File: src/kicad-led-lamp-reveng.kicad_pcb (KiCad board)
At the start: 2 copper layers, 18 parts, among them J1 AC2, J2 AC1, J3 L+, J4 L-, SW1 SW_Push_SPDT

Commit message: Finished pcb layout
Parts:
- removed the R1 at (84.7, 77.9)
- added R3: 390k, Resistor_THT:R_Axial_DIN0207_L6.3mm_D2.5mm_P7.62mm_Horizontal, F.Cu at (128.3, 85.7)
- D1, D3, D4, D5, D6: footprint Resistor_THT:R_Axial_DIN0207_L6.3mm_D2.5mm_P7.62mm_Horizontal -> igorkelvin:DIODE_Axial_DIN0207_L6.3mm_D2.5mm_P7.62mm_Horizontal
- moved C1 117.6 mm to (178.4, 74.9), turned to 270 degrees
- moved R1 109.5 mm to (183.5, 74.9), turned to 270 degrees
- moved C2 108.4 mm to (168.3, 92.7), turned to 180 degrees
- moved R2 106.4 mm to (167.0, 77.5), turned to 270 degrees
- moved D1 101.2 mm to (172.1, 77.5), turned to 270 degrees
- moved D4 81.0 mm to (142.2, 95.2), turned to 90 degrees
- moved D5 79.3 mm to (139.1, 77.5), turned to 270 degrees
- moved SW1 75.7 mm to (149.2, 85.1)
- moved D6 67.4 mm to (139.1, 95.2), turned to 90 degrees
- moved D2 64.3 mm to (159.4, 71.1), turned to 180 degrees
- moved J2 62.0 mm to (145.4, 88.9)
- moved J1 61.4 mm to (147.3, 75.6)
- moved R4 60.8 mm to (145.4, 77.5), turned to 270 degrees
- moved D3 48.1 mm to (142.2, 85.1), turned to 90 degrees
- moved C3 44.1 mm to (129.7, 78.7)
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- renumbered R3 to R1
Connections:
- D5 pad 2: Net-(C1-Pad2) -> Net-(D5-Pad2)
- R4 pad 2: Net-(C1-Pad2) -> Net-(D5-Pad2)
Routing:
- net Net-(C3-Pad1): track 0.00 -> 113.3 mm
- net Net-(C1-Pad2): track 0.00 -> 77.5 mm
- net Net-(C3-Pad2): track 0.00 -> 28.0 mm
- net Net-(C1-Pad1): track 0.00 -> 25.3 mm
- net Net-(D2-Pad2): track 0.00 -> 23.8 mm
- net Net-(C2-Pad1): track 0.00 -> 13.2 mm
- net Net-(J1-Pad1): track 0.00 -> 11.9 mm
- net Net-(D5-Pad2): track 0.00 -> 10.3 mm
- net Net-(D3-Pad1): track 0.00 -> 6.24 mm
- added copper zone on B.Cu, net Net-(C1-Pad1)
- added copper zone on B.Cu, net Net-(C1-Pad2)
- added copper zone on B.Cu, net Net-(C2-Pad1)
- added copper zone on B.Cu, net Net-(C3-Pad1)
- added copper zone on B.Cu, net Net-(C3-Pad2)
- added copper zone on B.Cu, net Net-(D2-Pad2)
- added copper zone on B.Cu, net Net-(D3-Pad1)
- added copper zone on B.Cu, net Net-(D5-Pad2)
- added copper zone on B.Cu, net Net-(J1-Pad1)
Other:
- board outline added: 63.2 x 31.1 mm
- net class asd added: clearance 0.2, trace_width 1, via_dia 0.8, via_drill 0.4

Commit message: Schematics rearrangement, changed C3 polarity and Rev1 for pcb & sch
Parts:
- C1: value 220nF_400V_Polyester -> 220nF
- C2: value 1uF_400V_Polyester -> 1uF
- C3: value 6.8uF_400V_Electrolytic -> 6.8uF
- D2: value LED_ALT -> LED
- moved C3 4.95 mm to (134.6, 78.7), turned to 180 degrees
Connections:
- D1 pad 2: Net-(C3-Pad1) -> Net-(C3-Pad2)
- D2 pad 1: Net-(C3-Pad1) -> Net-(C3-Pad2)
- D3 pad 1: Net-(D3-Pad1) -> Net-(C3-Pad2)
- D3 pad 2: Net-(C3-Pad1) -> Net-(D3-Pad2)
- D4 pad 1: Net-(C3-Pad2) -> Net-(C3-Pad1)
- D4 pad 2: Net-(D3-Pad1) -> Net-(D3-Pad2)
- D6 pad 1: Net-(C3-Pad2) -> Net-(C3-Pad1)
- J2 pad 1: Net-(D3-Pad1) -> Net-(D3-Pad2)
- J3 pad 1: Net-(C3-Pad2) -> Net-(C3-Pad1)
- J4 pad 1: Net-(C3-Pad1) -> Net-(C3-Pad2)
- R3 pad 1: Net-(C3-Pad1) -> Net-(C3-Pad2)
- R3 pad 2: Net-(C3-Pad2) -> Net-(C3-Pad1)
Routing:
- net Net-(C3-Pad2): track 28.0 -> 113.3 mm
- net Net-(C3-Pad1): track 113.3 -> 28.0 mm
- added copper zone on B.Cu, net Net-(D3-Pad2)
- removed copper zone on B.Cu, net Net-(C2-Pad1)
- removed copper zone on B.Cu, net Net-(C3-Pad2)
- removed copper zone on B.Cu, net Net-(D3-Pad1)

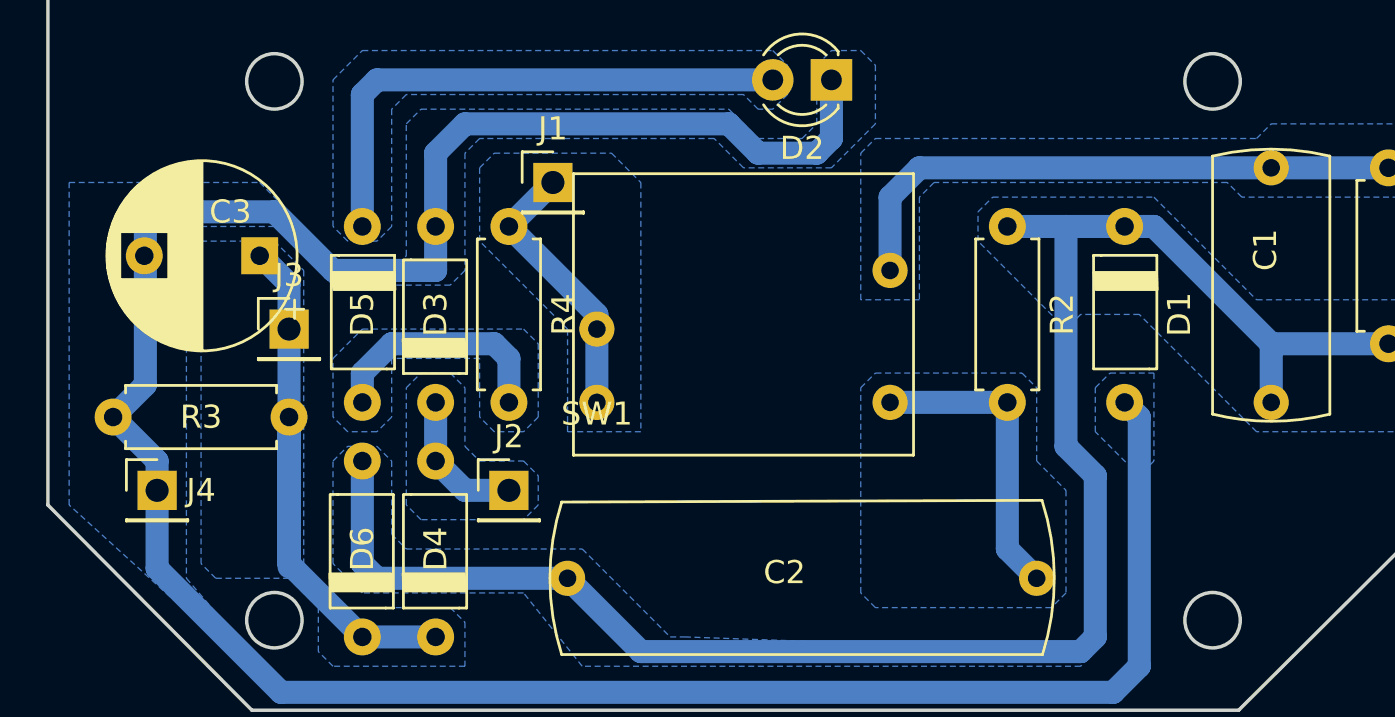
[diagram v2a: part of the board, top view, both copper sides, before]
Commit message: Corrected D3 and PCB filled zones
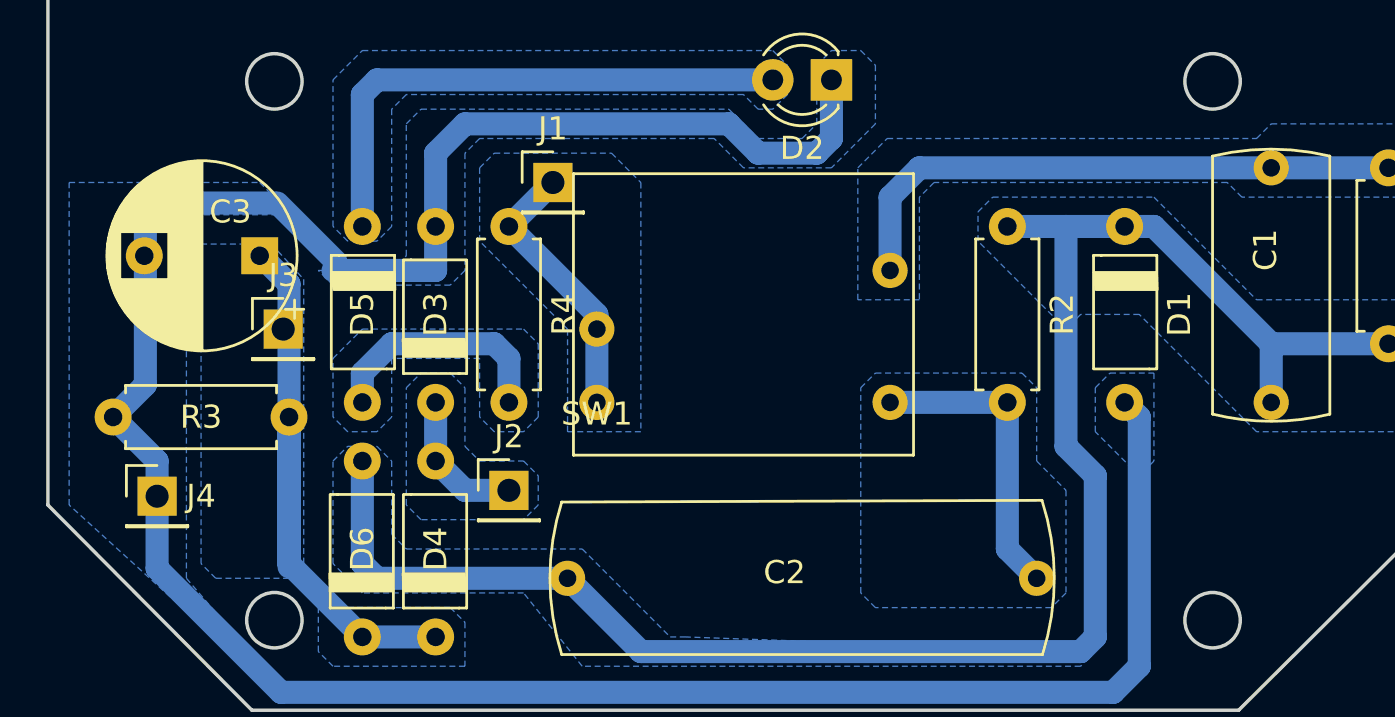
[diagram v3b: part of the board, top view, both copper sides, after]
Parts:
- moved J3 0.25 mm to (135.6, 81.9)
- moved J4 0.25 mm to (130.2, 89.2)
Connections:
- D3 pad 1: Net-(C3-Pad2) -> Net-(D3-Pad1)
- D3 pad 2: Net-(D3-Pad2) -> Net-(C3-Pad2)
- D4 pad 2: Net-(D3-Pad2) -> Net-(D3-Pad1)
- J2 pad 1: Net-(D3-Pad2) -> Net-(D3-Pad1)
- SW1 pad 4: (no net) -> Net-(J1-Pad1)
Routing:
- added copper zone on B.Cu, net Net-(C2-Pad1)
- added copper zone on B.Cu, net Net-(C3-Pad2)
- added copper zone on B.Cu, net Net-(D3-Pad1)
- removed copper zone on B.Cu, net Net-(D3-Pad2)
